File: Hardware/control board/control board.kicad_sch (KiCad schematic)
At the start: 9 parts, among them J1 Conn_01x03_Pin, J2 Conn_01x03_Pin, J3 Conn_01x03_Pin, J4 Conn_01x03_Pin, J5 Conn_01x03_Pin, J6 Conn_01x03_Pin, J7 Conn_01x03_Pin, J8 Conn_01x03_Pin

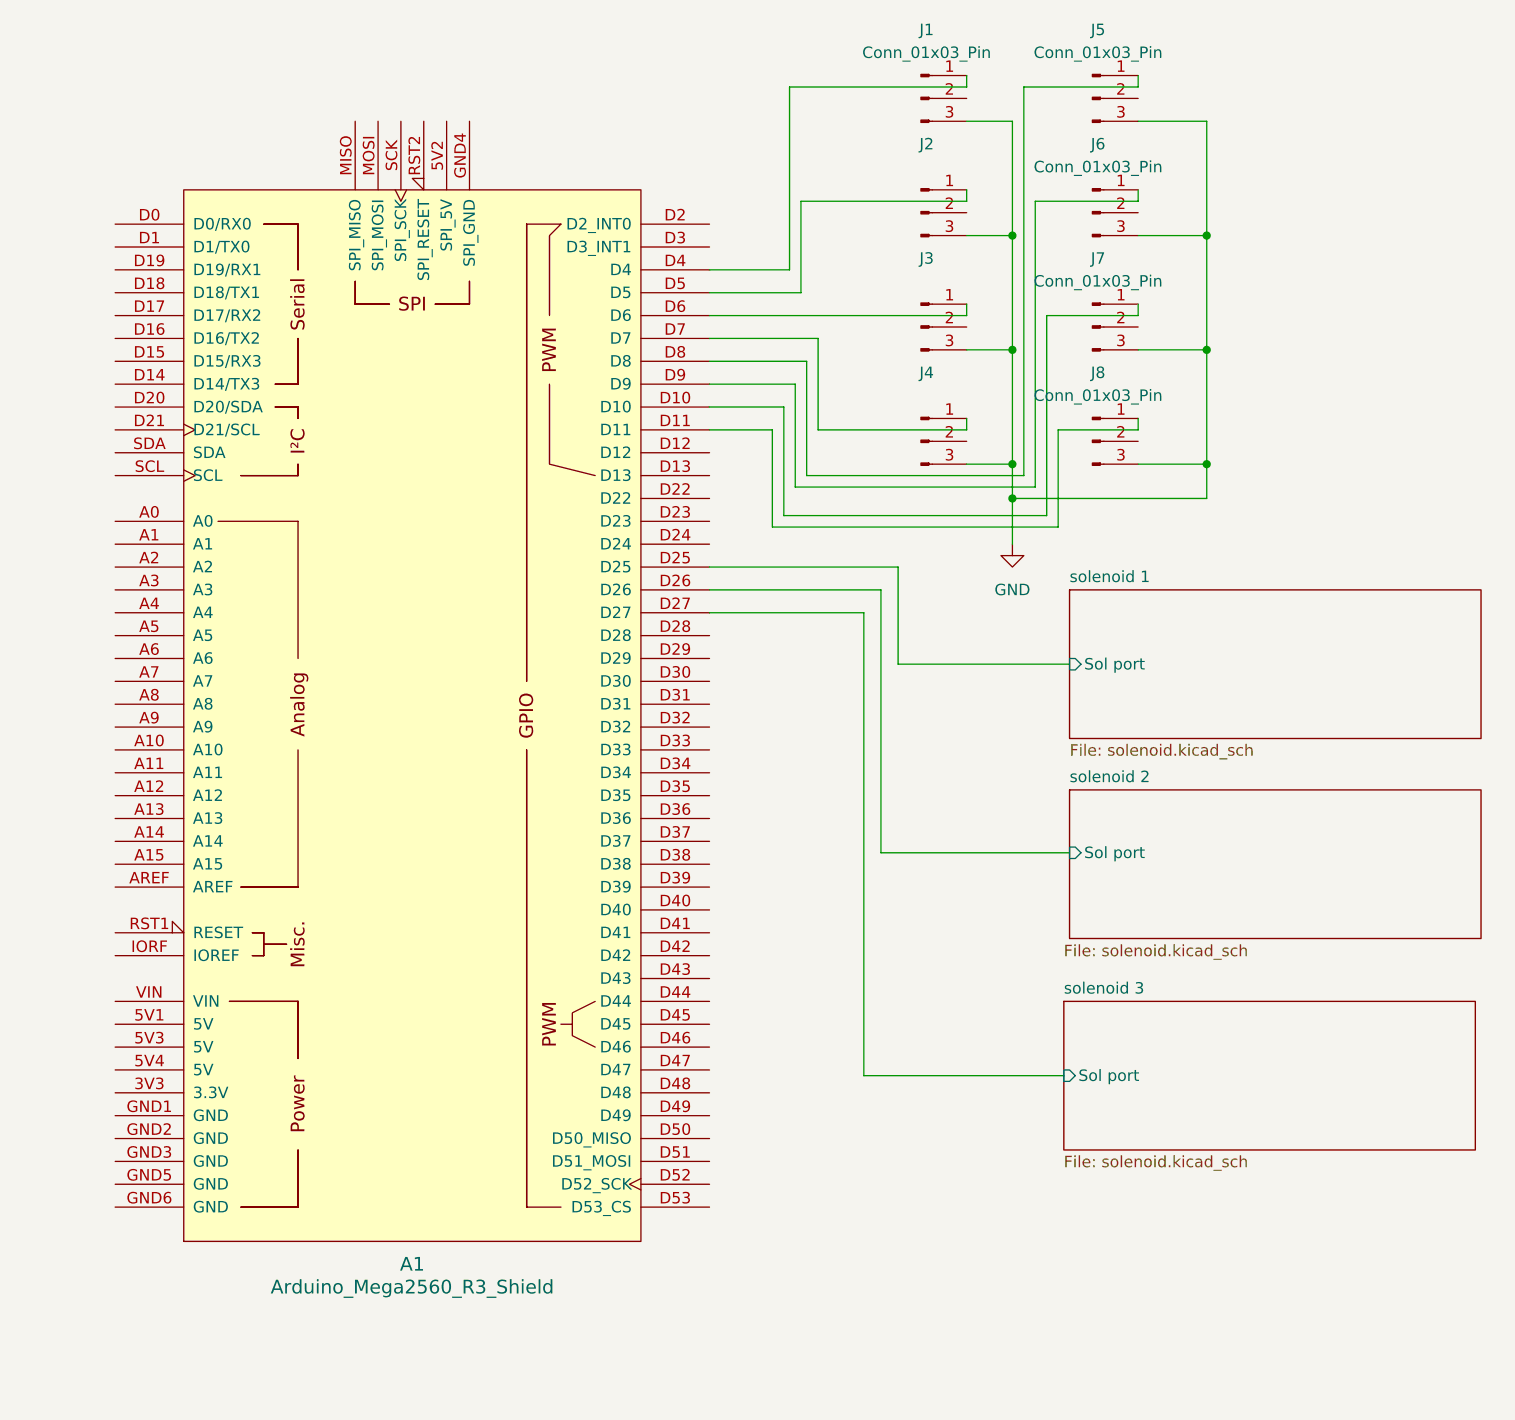
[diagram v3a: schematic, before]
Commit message: Revert "Merge branch 'hardware' of https://github.com/bruin-underwater-robotics/2023-2024 into hardware"
This reverts commit 2d92dd737ed49dde43700235594c19fac80c6213, reversing
changes made to 7ccd23260c988ead49c0bcfa936e50f6d09a7000.
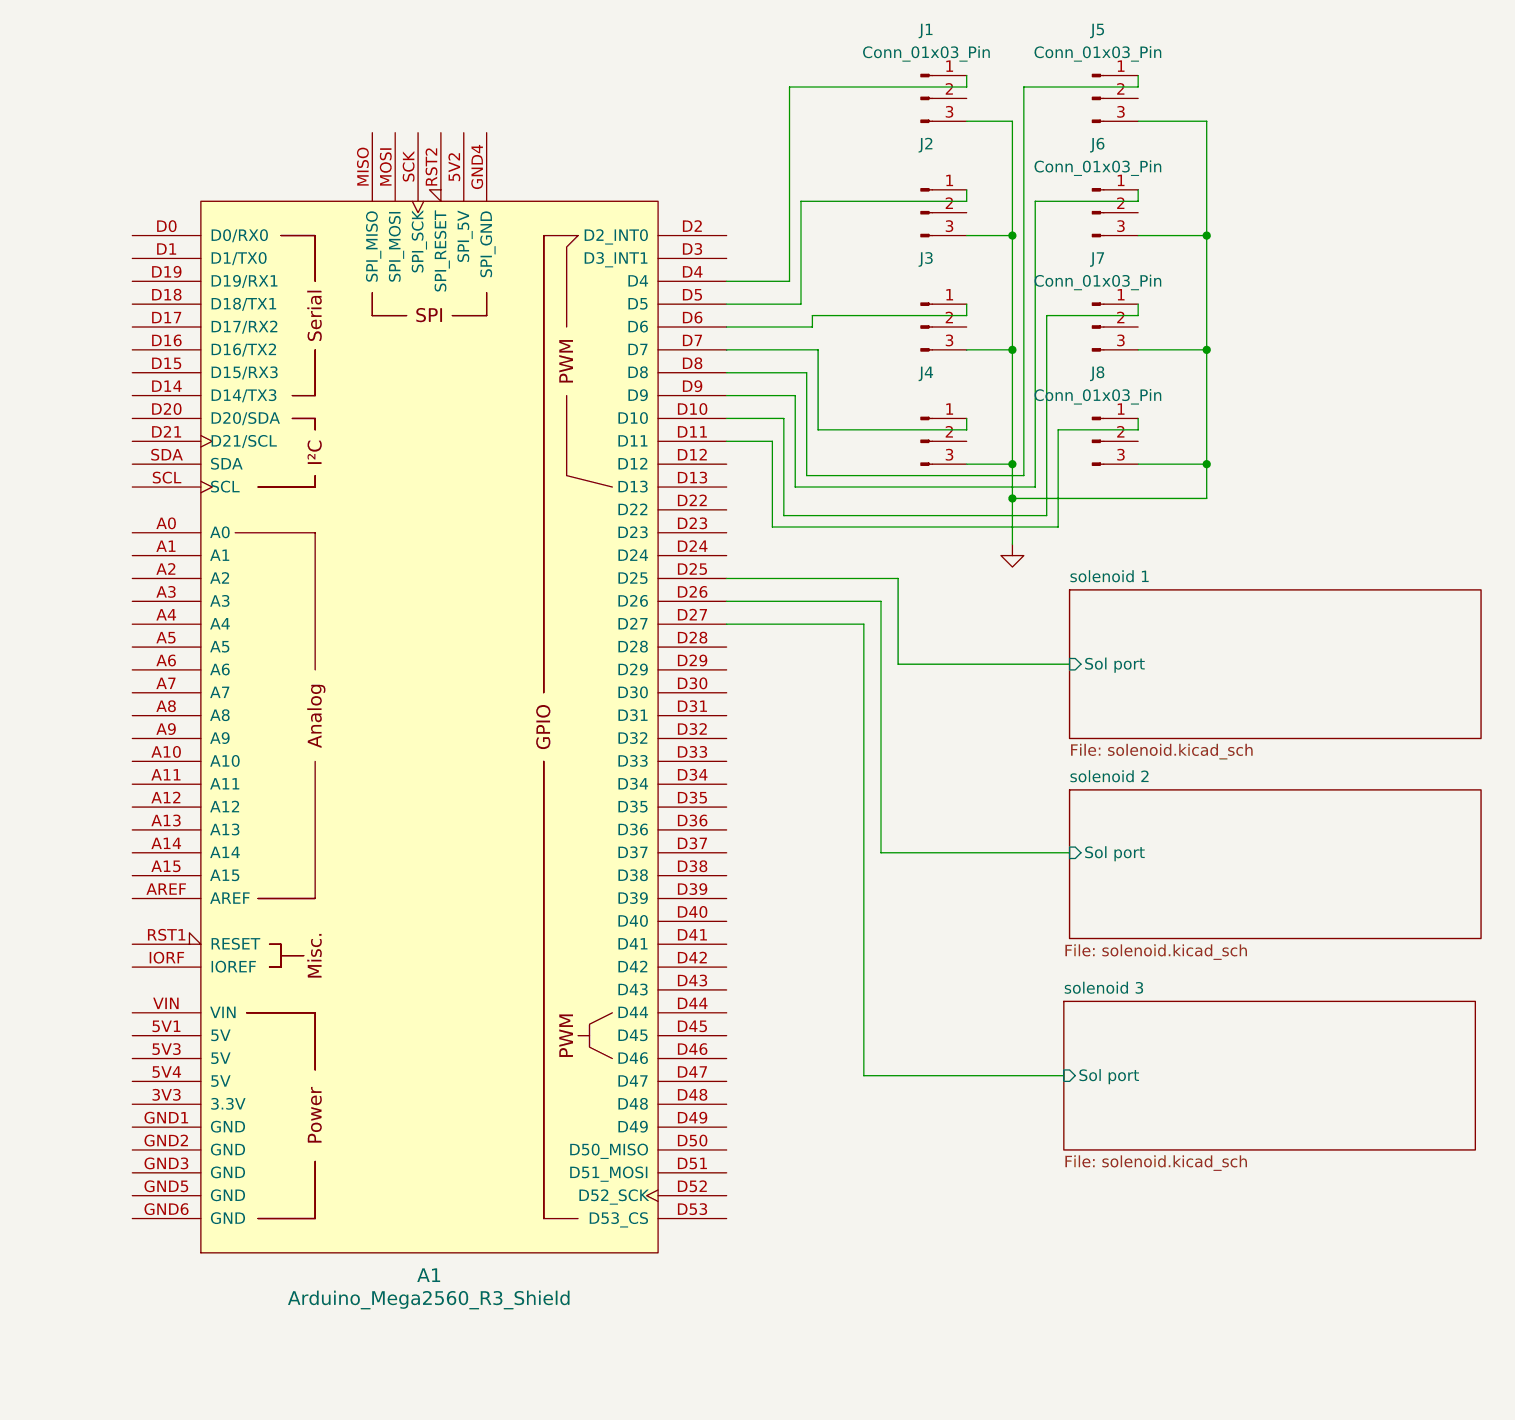
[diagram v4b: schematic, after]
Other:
- moved on the sheet: A1
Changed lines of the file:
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@@
     (stroke (width 0) (type default))
   )
-  (wire (pts (xy 91.44 46.99) (xy 120.015 46.99))
+  (wire (pts (xy 102.87 46.99) (xy 120.015 46.99))
     (stroke (width 0) (type default))
   )
@@
     (stroke (width 0) (type default))
   )
-  (wire (pts (xy 99.695 57.15) (xy 91.44 57.15))
+  (wire (pts (xy 99.695 58.42) (xy 93.345 58.42))
     (stroke (width 0) (type default))
   )
@@
     (stroke (width 0) (type default))
   )
-  (wire (pts (xy 112.395 74.93) (xy 112.395 85.725))
+  (wire (pts (xy 112.395 85.725) (xy 112.395 76.2))
     (stroke (width 0) (type default))
   )
@@
     (stroke (width 0) (type default))
   )
-  (wire (pts (xy 112.395 74.93) (xy 91.44 74.93))
+  (wire (pts (xy 112.395 76.2) (xy 93.345 76.2))
     (stroke (width 0) (type default))
   )
@@
     (stroke (width 0) (type default))
   )
-  (wire (pts (xy 101.6 44.45) (xy 91.44 44.45))
-    (stroke (width 0) (type default))
-  )
-  (wire (pts (xy 102.235 64.77) (xy 102.235 52.07))
-    (stroke (width 0) (type default))
-  )
-  (wire (pts (xy 100.33 41.91) (xy 100.33 21.59))
-    (stroke (width 0) (type default))
-  )
-  (wire (pts (xy 99.695 69.215) (xy 99.695 57.15))
+  (wire (pts (xy 101.6 45.72) (xy 93.345 45.72))
+    (stroke (width 0) (type default))
+  )
+  (wire (pts (xy 102.235 64.77) (xy 102.235 53.34))
+    (stroke (width 0) (type default))
+  )
+  (wire (pts (xy 100.33 21.59) (xy 100.33 43.18))
+    (stroke (width 0) (type default))
+  )
+  (wire (pts (xy 99.695 69.215) (xy 99.695 58.42))
     (stroke (width 0) (type default))
   )
@@
     (stroke (width 0) (type default))
   )
-  (wire (pts (xy 103.505 49.53) (xy 103.505 59.69))
+  (wire (pts (xy 103.505 59.69) (xy 103.505 50.8))
     (stroke (width 0) (type default))
   )
@@
     (stroke (width 0) (type default))
   )
-  (wire (pts (xy 98.425 59.69) (xy 91.44 59.69))
+  (wire (pts (xy 98.425 60.96) (xy 93.345 60.96))
     (stroke (width 0) (type default))
   )
@@
     (stroke (width 0) (type default))
   )
-  (wire (pts (xy 102.235 52.07) (xy 91.44 52.07))
-    (stroke (width 0) (type default))
-  )
-  (wire (pts (xy 108.585 131.445) (xy 108.585 80.01))
+  (wire (pts (xy 102.235 53.34) (xy 93.345 53.34))
+    (stroke (width 0) (type default))
+  )
+  (wire (pts (xy 108.585 131.445) (xy 108.585 81.28))
     (stroke (width 0) (type default))
   )
@@
     (stroke (width 0) (type default))
   )
-  (wire (pts (xy 100.965 66.04) (xy 100.965 54.61))
+  (wire (pts (xy 100.965 66.04) (xy 100.965 55.88))
     (stroke (width 0) (type default))
   )
@@
     (stroke (width 0) (type default))
   )
-  (wire (pts (xy 110.49 77.47) (xy 91.44 77.47))
+  (wire (pts (xy 110.49 78.74) (xy 93.345 78.74))
     (stroke (width 0) (type default))
   )
@@
     (stroke (width 0) (type default))
   )
-  (wire (pts (xy 100.33 41.91) (xy 91.44 41.91))
+  (wire (pts (xy 100.33 43.18) (xy 93.345 43.18))
+    (stroke (width 0) (type default))
+  )
+  (wire (pts (xy 102.87 46.99) (xy 102.87 48.26))
     (stroke (width 0) (type default))
   )
@@
     (stroke (width 0) (type default))
   )
-  (wire (pts (xy 110.49 106.68) (xy 110.49 77.47))
+  (wire (pts (xy 110.49 106.68) (xy 110.49 78.74))
     (stroke (width 0) (type default))
   )
@@
     (stroke (width 0) (type default))
   )
-  (wire (pts (xy 101.6 44.45) (xy 101.6 34.29))
-    (stroke (width 0) (type default))
-  )
-  (wire (pts (xy 103.505 49.53) (xy 91.44 49.53))
-    (stroke (width 0) (type default))
-  )
-  (wire (pts (xy 98.425 59.69) (xy 98.425 70.485))
+  (wire (pts (xy 101.6 34.29) (xy 101.6 45.72))
+    (stroke (width 0) (type default))
+  )
+  (wire (pts (xy 103.505 50.8) (xy 93.345 50.8))
+    (stroke (width 0) (type default))
+  )
+  (wire (pts (xy 98.425 70.485) (xy 98.425 60.96))
     (stroke (width 0) (type default))
   )
@@
     (stroke (width 0) (type default))
   )
-  (wire (pts (xy 108.585 80.01) (xy 91.44 80.01))
+  (wire (pts (xy 108.585 81.28) (xy 93.345 81.28))
+    (stroke (width 0) (type default))
+  )
+  (wire (pts (xy 102.87 48.26) (xy 93.345 48.26))
     (stroke (width 0) (type default))
   )
@@
     (stroke (width 0) (type default))
   )
-  (wire (pts (xy 100.965 54.61) (xy 91.44 54.61))
-    (stroke (width 0) (type default))
-  )
-  (symbol (lib_id "PCM_arduino-library:Arduino_Mega2560_R3_Shield") (at 58.42 91.44 0) (unit 1)
+  (wire (pts (xy 100.965 55.88) (xy 93.345 55.88))
+    (stroke (width 0) (type default))
+  )
+  (symbol (lib_id "power:GND") (at 125.095 72.39 0) (unit 1)
     (in_bom yes) (on_board yes) (dnp no) (fields_autoplaced)
-    (property "Reference" "A1" (at 58.42 152.4 0)
+    (property "Reference" "#PWR01" (at 125.095 78.74 0)
+      (effects (font (size 1.27 1.27)) hide)
+    )
+    (property "Value" "GND" (at 125.095 77.47 0)
+      (effects (font (size 1.27 1.27)) hide)
+    )
+    (property "Footprint" "" (at 125.095 72.39 0)
+      (effects (font (size 1.27 1.27)) hide)
+    )
+    (property "Datasheet" "" (at 125.095 72.39 0)
+      (effects (font (size 1.27 1.27)) hide)
+    )
+    (pin "1")
+    (instances
+      (project "control board"
+        (path "/cf0863a8-7f64-449b-8eb4-3c06c871fb37"
+          (reference "#PWR01") (unit 1)
+        )
+      )
+    )
+  )
+  (symbol (lib_id "PCM_arduino-library:Arduino_Mega2560_R3_Shield") (at 60.325 92.71 0) (unit 1)
+    (in_bom yes) (on_board yes) (dnp no) (fields_autoplaced)
+    (property "Reference" "A1" (at 60.325 153.67 0)
       (effects (font (size 1.524 1.524)))
     )
-    (property "Value" "Arduino_Mega2560_R3_Shield" (at 58.42 154.94 0)
+    (property "Value" "Arduino_Mega2560_R3_Shield" (at 60.325 156.21 0)
       (effects (font (size 1.524 1.524)))
     )
-    (property "Footprint" "PCM_arduino-library:Arduino_Mega2560_R3_Shield" (at 58.42 165.1 0)
+    (property "Footprint" "PCM_arduino-library:Arduino_Mega2560_R3_Shield" (at 60.325 166.37 0)
       (effects (font (size 1.524 1.524)) hide)
     )
-    (property "Datasheet" "https://docs.arduino.cc/hardware/mega-2560" (at 58.42 161.29 0)
+    (property "Datasheet" "https://docs.arduino.cc/hardware/mega-2560" (at 60.325 162.56 0)
       (effects (font (size 1.524 1.524)) hide)
     )
@@
         )
       )
-    )
-  )
-  (symbol (lib_id "power:GND") (at 125.095 72.39 0) (unit 1)
-    (in_bom yes) (on_board yes) (dnp no) (fields_autoplaced)
-    (property "Reference" "#PWR02" (at 125.095 78.74 0)
-      (effects (font (size 1.27 1.27)) hide)
-    )
-    (property "Value" "GND" (at 125.095 77.47 0)
-      (effects (font (size 1.27 1.27)))
-    )
-    (property "Footprint" "" (at 125.095 72.39 0)
-      (effects (font (size 1.27 1.27)) hide)
-    )
-    (property "Datasheet" "" (at 125.095 72.39 0)
-      (effects (font (size 1.27 1.27)) hide)
-    )
-    (pin "1")
-    (instances
-      (project "control board"
-        (path "/cf0863a8-7f64-449b-8eb4-3c06c871fb37"
-          (reference "#PWR02") (unit 1)
-        )
-      )

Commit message: revised control board design and updated voltage indicators
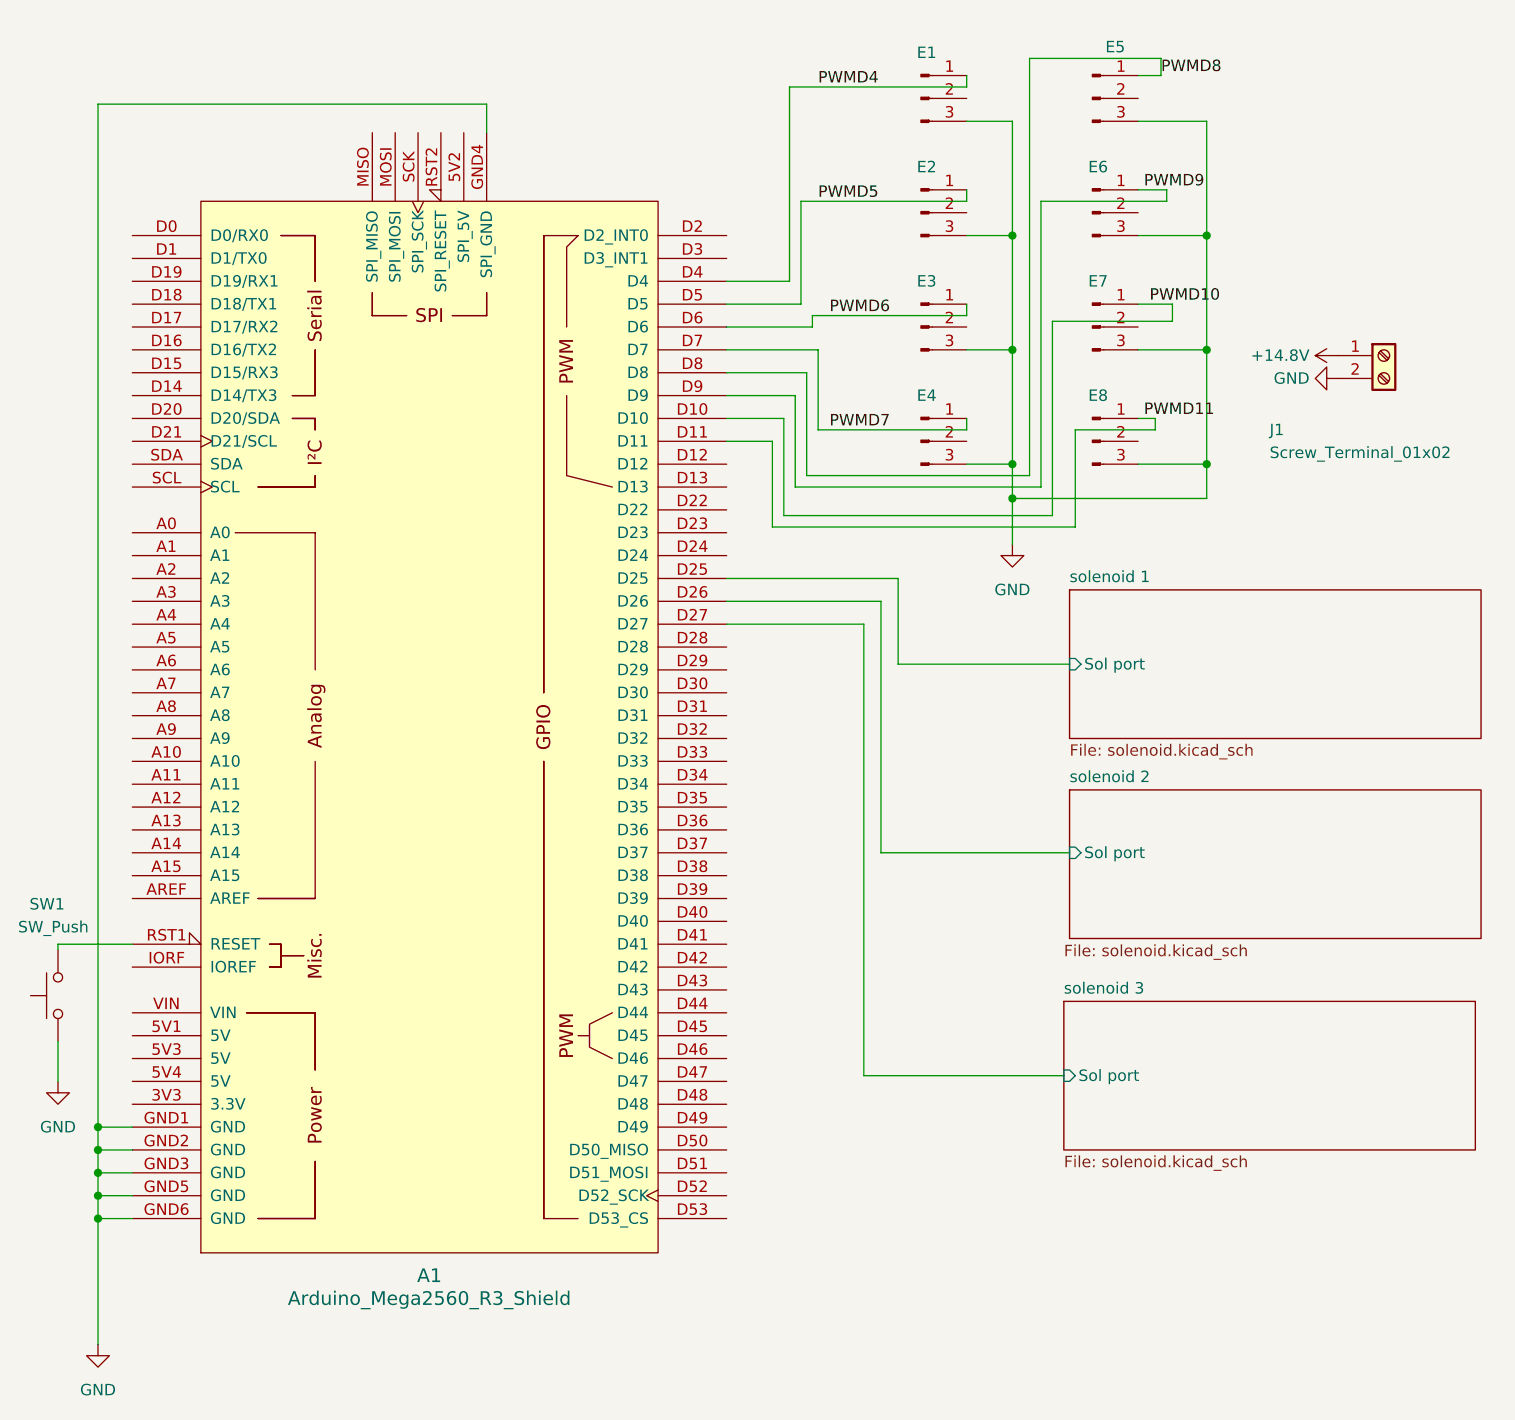
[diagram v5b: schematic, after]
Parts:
- added J1: Screw_Terminal_01x02, symbol Connector:Screw_Terminal_01x02
- added SW1: SW_Push, symbol Switch:SW_Push
- renumbered J1 to E1, J2 to E2, J3 to E3, J4 to E4, J5 to E5, J6 to E6, J7 to E7, J8 to E8
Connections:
- net GND: now also A1.GND1 (GND), A1.GND2 (GND), A1.GND3 (GND), A1.GND4 (SPI_GND), A1.GND5 (GND), A1.GND6 (GND), J1.2 (Pin_2), SW1.1
- net PWMD10: now reaches A1.D10, E7.1 (Pin_1)
- net PWMD11: now reaches A1.D11, E8.1 (Pin_1)
- net PWMD4: now reaches A1.D4, E1.1 (Pin_1)
- net PWMD5: now reaches A1.D5, E2.1 (Pin_1)
- net PWMD6: now reaches A1.D6, E3.1 (Pin_1)
- net PWMD7: now reaches A1.D7, E4.1 (Pin_1)
- net PWMD8: now reaches A1.D8, E5.1 (Pin_1)
- net PWMD9: now reaches A1.D9, E6.1 (Pin_1)
- net at A1.RST1 (RESET): now also SW1.2
- new net +14.8V: J1.1 (Pin_1)
